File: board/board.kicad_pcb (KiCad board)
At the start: 2 copper layers, 36.5 x 17.5 mm, 41 parts, among them J2 Conn_01x10, J3 Conn_01x06, J4 Conn_01x02, J7 Conn_01x30, J8 USB_C_Receptacle_USB2.0_16P, J9 Conn_01x02, U2 nPM1300-QEAA, U3 MDBT50Q-P1MV2, U4 TVS_Array, Y1 32k Hz

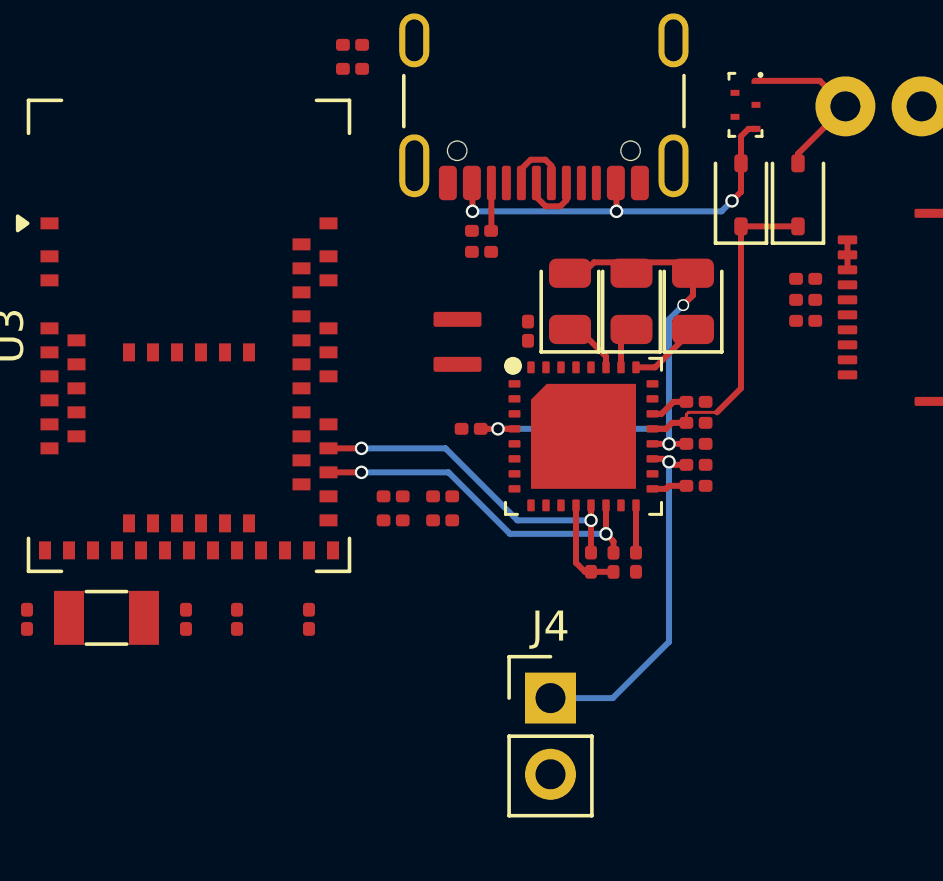
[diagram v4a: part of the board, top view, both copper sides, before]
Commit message: board: pcb route cc and vbus
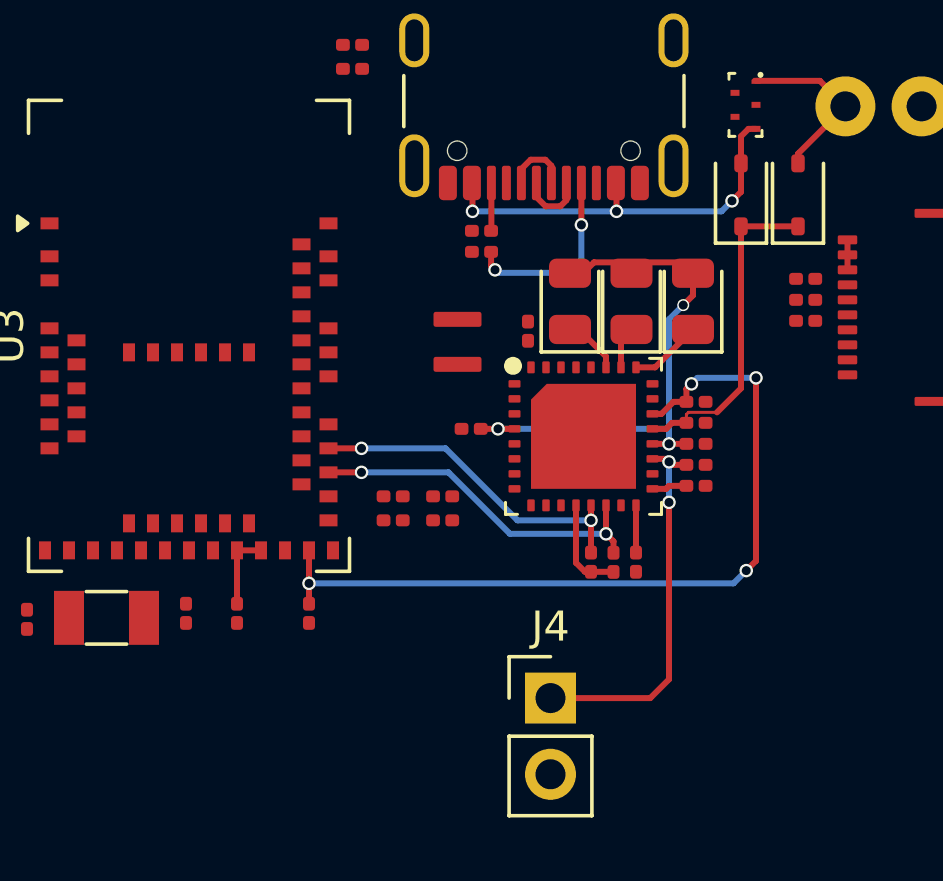
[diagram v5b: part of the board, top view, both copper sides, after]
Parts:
- moved C10 0.20 mm to (101.5, 67.2)
- moved C7 0.20 mm to (99.8, 67.2)
- moved C9 0.20 mm to (103.8, 67.2)
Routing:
- net vbus: track 1.30 -> 27.3 mm, vias 0 -> 4
- net Net-(J8-CC1): track 0.00 -> 6.33 mm, vias 0 -> 2
- net +3V3: track 3.29 -> 5.87 mm
- net vbat: track 11.9 -> 12.7 mm, vias 1 -> 2
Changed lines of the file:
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@@
 	(footprint "Capacitor_SMD:C_0201_0603Metric"
 		(layer "F.Cu")
-		(at 99.75 67.4 -90)
+		(at 99.75 67.2 -90)
 		(descr "Capacitor SMD 0201 (0603 Metric), square (rectangular) end terminal, IPC-7351 nominal, (Body size source: https://www.vishay.com/docs/20052/crcw0201e3.pdf), generated with kicad-footprint-generator")
 		(tags "capacitor")
@@
 	(footprint "Capacitor_SMD:C_0201_0603Metric"
 		(layer "F.Cu")
-		(at 103.85 67.4 -90)
+		(at 103.85 67.2 -90)
 		(descr "Capacitor SMD 0201 (0603 Metric), square (rectangular) end terminal, IPC-7351 nominal, (Body size source: https://www.vishay.com/docs/20052/crcw0201e3.pdf), generated with kicad-footprint-generator")
 		(tags "capacitor")
@@
 	(footprint "Capacitor_SMD:C_0201_0603Metric"
 		(layer "F.Cu")
-		(at 101.45 67.4 90)
+		(at 101.45 67.2 90)
 		(descr "Capacitor SMD 0201 (0603 Metric), square (rectangular) end terminal, IPC-7351 nominal, (Body size source: https://www.vishay.com/docs/20052/crcw0201e3.pdf), generated with kicad-footprint-generator")
 		(tags "capacitor")
@@
 	)
 	(segment
+		(start 103.85 66.88)
+		(end 103.85 66.2)
+		(width 0.2)
+		(layer "F.Cu")
+		(net 3)
+	)
+	(segment
+		(start 116.43 59.72)
+		(end 116.6 59.55)
+		(width 0.2)
+		(layer "F.Cu")
+		(net 3)
+	)
+	(segment
+		(start 118.75 65.45)
+		(end 118.75 59.35)
+		(width 0.2)
+		(layer "F.Cu")
+		(net 3)
+	)
+	(segment
+		(start 118.425 65.775)
+		(end 118.75 65.45)
+		(width 0.2)
+		(layer "F.Cu")
+		(net 3)
+	)
+	(segment
+		(start 116.425 60.145)
+		(end 116.43 60.15)
+		(width 0.2)
+		(layer "F.Cu")
+		(net 3)
+	)
+	(segment
+		(start 103.85 66.2)
+		(end 103.85 65.1)
+		(width 0.2)
+		(layer "F.Cu")
+		(net 3)
+	)
+	(segment
+		(start 116.43 60.15)
+		(end 116.43 59.72)
+		(width 0.2)
+		(layer "F.Cu")
+		(net 3)
+	)
+	(segment
 		(start 115.3 60.55)
 		(end 115.6 60.55)
@@
 		(net 3)
 	)
+	(via
+		(at 118.75 59.35)
+		(size 0.45)
+		(drill 0.3)
+		(layers "F.Cu" "B.Cu")
+		(net 3)
+	)
+	(via
+		(at 116.6 59.55)
+		(size 0.45)
+		(drill 0.3)
+		(layers "F.Cu" "B.Cu")
+		(net 3)
+	)
+	(via
+		(at 103.85 66.2)
+		(size 0.45)
+		(drill 0.3)
+		(layers "F.Cu" "B.Cu")
+		(net 3)
+	)
+	(via
+		(at 118.425 65.775)
+		(size 0.45)
+		(drill 0.3)
+		(layers "F.Cu" "B.Cu")
+		(net 3)
+	)
+	(segment
+		(start 118 66.2)
+		(end 103.85 66.2)
+		(width 0.2)
+		(layer "B.Cu")
+		(net 3)
+	)
+	(segment
+		(start 118.75 59.35)
+		(end 116.8 59.35)
+		(width 0.2)
+		(layer "B.Cu")
+		(net 3)
+	)
+	(segment
+		(start 116.8 59.35)
+		(end 116.6 59.55)
+		(width 0.2)
+		(layer "B.Cu")
+		(net 3)
+	)
+	(segment
+		(start 118.425 65.775)
+		(end 118 66.2)
+		(width 0.2)
+		(layer "B.Cu")
+		(net 3)
+	)
 	(segment
 		(start 115.95 60.85)
@@
 	)
 	(segment
+		(start 115.85 69.4)
+		(end 115.85 63.5)
+		(width 0.2)
+		(layer "F.Cu")
+		(net 5)
+	)
+	(segment
 		(start 115.3 62.05)
 		(end 115.75 62.05)
@@
 	)
 	(segment
+		(start 111.9 70.025)
+		(end 115.225 70.025)
+		(width 0.2)
+		(layer "F.Cu")
+		(net 5)
+	)
+	(segment
 		(start 115.95 62.25)
 		(end 116.43 62.25)
@@
 		(net 5)
 	)
+	(segment
+		(start 115.225 70.025)
+		(end 115.85 69.4)
+		(width 0.2)
+		(layer "F.Cu")
+		(net 5)
+	)
 	(via
 		(at 115.85 62.15)
@@
 		(net 5)
 	)
-	(segment
-		(start 113.975 70.025)
-		(end 111.9 70.025)
-		(width 0.2)
-		(layer "B.Cu")
+	(via
+		(at 115.85 63.5)
+		(size 0.45)
+		(drill 0.3)
+		(layers "F.Cu" "B.Cu")
 		(net 5)
 	)
 	(segment
 		(start 115.85 62.15)
-		(end 115.85 68.15)
-		(width 0.2)
-		(layer "B.Cu")
-		(net 5)
-	)
-	(segment
-		(start 115.85 68.15)
-		(end 113.975 70.025)
+		(end 115.85 63.5)
 		(width 0.2)
 		(layer "B.Cu")
@@
 	)
 	(segment
+		(start 101.45 65.1)
+		(end 101.45 66.88)
+		(width 0.2)
+		(layer "F.Cu")
+		(net 46)
+	)
+	(segment
 		(start 112.75 65.514999)
 		(end 113.050001 65.815)
@@
 	)
 	(segment
+		(start 102.25 65.1)
+		(end 101.45 65.1)
+		(width 0.2)
+		(layer "F.Cu")
+		(net 46)
+	)
+	(segment
 		(start 112.75 63.6)
 		(end 112.75 65.514999)
@@
 		(net 71)
 	)
+	(segment
+		(start 110.05 55.75)
+		(end 109.92 55.62)
+		(width 0.2)
+		(layer "F.Cu")
+		(net 74)
+	)
+	(segment
+		(start 112.93 52.855)
+		(end 112.93 54.22)
+		(width 0.2)
+		(layer "F.Cu")
+		(net 74)
+	)
+	(segment
+		(start 112.93 54.22)
+		(end 112.9 54.25)
+		(width 0.2)
+		(layer "F.Cu")
+		(net 74)
+	)
+	(segment
+		(start 109.92 55.62)
+		(end 109.92 55.15)
+		(width 0.2)
+		(layer "F.Cu")
+		(net 74)
+	)
+	(via
+		(at 110.05 55.75)
+		(size 0.45)
+		(drill 0.3)
+		(layers "F.Cu" "B.Cu")
+		(net 74)
+	)
+	(via
+		(at 112.93 54.25)
+		(size 0.45)
+		(drill 0.3)
+		(layers "F.Cu" "B.Cu")
+		(net 74)
+	)
+	(segment
+		(start 112.93 55.42)
+		(end 112.93 54.25)
+		(width 0.2)
+		(layer "B.Cu")
+		(net 74)
+	)
+	(segment
+		(start 110.05 55.75)
+		(end 110.15 55.85)
+		(width 0.2)
+		(layer "B.Cu")
+		(net 74)
+	)
+	(segment
+		(start 112.5 55.85)
+		(end 112.93 55.42)
+		(width 0.2)
+		(layer "B.Cu")
+		(net 74)
+	)
+	(segment
+		(start 110.15 55.85)
+		(end 112.5 55.85)
+		(width 0.2)
+		(layer "B.Cu")
+		(net 74)
+	)
 	(embedded_fonts no)

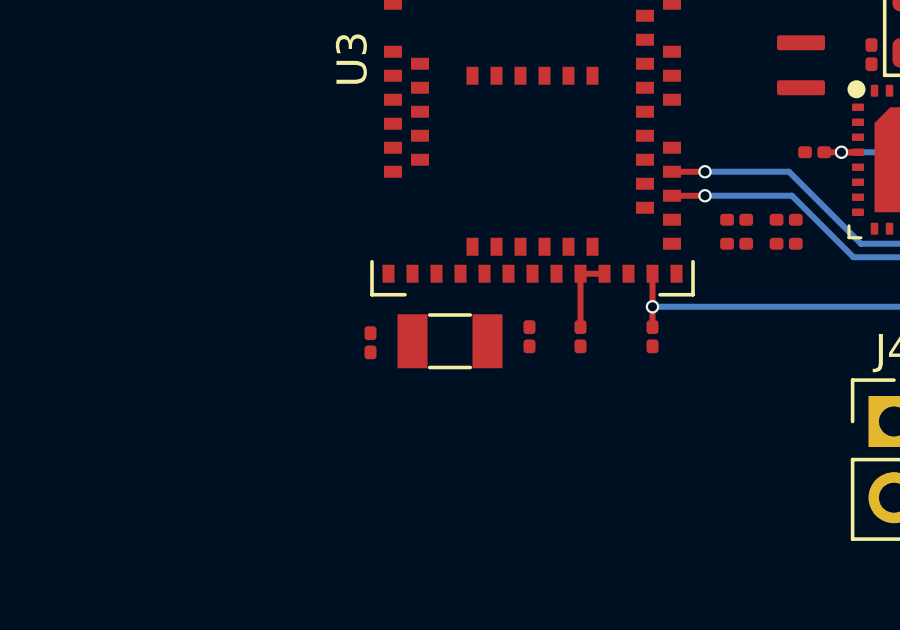
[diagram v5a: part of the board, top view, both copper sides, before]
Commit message: board: pcb route crystal
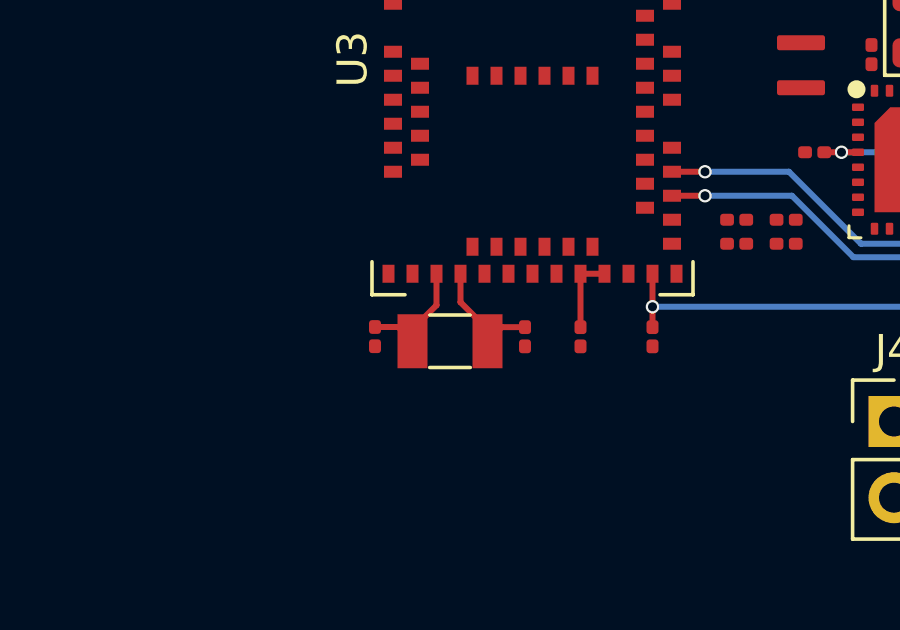
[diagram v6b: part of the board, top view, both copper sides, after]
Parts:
- moved C8 0.25 mm to (94.6, 67.2)
- moved C7 0.15 mm to (99.6, 67.2)
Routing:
- net Net-(U3-P0.01): track 0.00 -> 4.07 mm
- net Net-(U3-P0.00): track 0.00 -> 4.03 mm
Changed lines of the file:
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@@
 	(footprint "Capacitor_SMD:C_0201_0603Metric"
 		(layer "F.Cu")
-		(at 99.75 67.2 -90)
+		(at 99.6 67.2 -90)
 		(descr "Capacitor SMD 0201 (0603 Metric), square (rectangular) end terminal, IPC-7351 nominal, (Body size source: https://www.vishay.com/docs/20052/crcw0201e3.pdf), generated with kicad-footprint-generator")
 		(tags "capacitor")
@@
 	(footprint "Capacitor_SMD:C_0201_0603Metric"
 		(layer "F.Cu")
-		(at 94.45 67.4 -90)
+		(at 94.6 67.195 -90)
 		(descr "Capacitor SMD 0201 (0603 Metric), square (rectangular) end terminal, IPC-7351 nominal, (Body size source: https://www.vishay.com/docs/20052/crcw0201e3.pdf), generated with kicad-footprint-generator")
 		(tags "capacitor")
@@
 	)
 	(segment
+		(start 97.45 65.1)
+		(end 97.45 66.05)
+		(width 0.2)
+		(layer "F.Cu")
+		(net 1)
+	)
+	(segment
+		(start 98.35 67.35)
+		(end 98.82 66.88)
+		(width 0.2)
+		(layer "F.Cu")
+		(net 1)
+	)
+	(segment
+		(start 98.82 66.88)
+		(end 99.6 66.88)
+		(width 0.2)
+		(layer "F.Cu")
+		(net 1)
+	)
+	(segment
+		(start 98.35 66.95)
+		(end 98.35 67.35)
+		(width 0.2)
+		(layer "F.Cu")
+		(net 1)
+	)
+	(segment
+		(start 97.45 66.05)
+		(end 98.35 66.95)
+		(width 0.2)
+		(layer "F.Cu")
+		(net 1)
+	)
+	(segment
+		(start 96.65 66.15)
+		(end 95.85 66.95)
+		(width 0.2)
+		(layer "F.Cu")
+		(net 2)
+	)
+	(segment
+		(start 96.65 65.1)
+		(end 96.65 66.15)
+		(width 0.2)
+		(layer "F.Cu")
+		(net 2)
+	)
+	(segment
+		(start 95.85 67.35)
+		(end 95.375 66.875)
+		(width 0.2)
+		(layer "F.Cu")
+		(net 2)
+	)
+	(segment
+		(start 95.375 66.875)
+		(end 94.6 66.875)
+		(width 0.2)
+		(layer "F.Cu")
+		(net 2)
+	)
+	(segment
+		(start 95.85 66.95)
+		(end 95.85 67.35)
+		(width 0.2)
+		(layer "F.Cu")
+		(net 2)
+	)
+	(segment

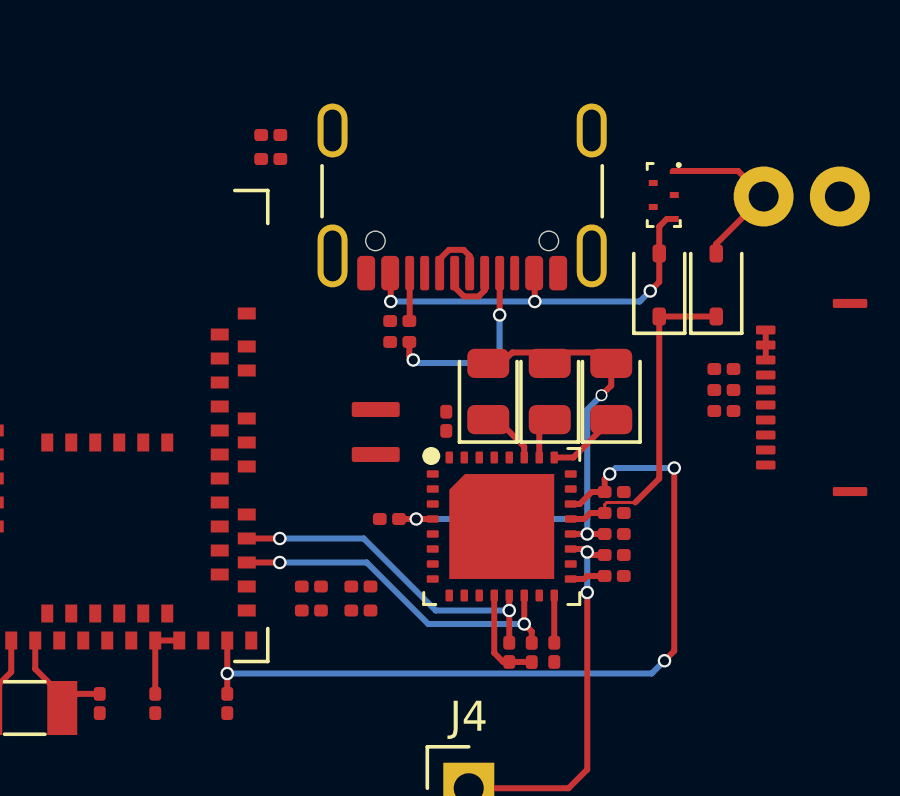
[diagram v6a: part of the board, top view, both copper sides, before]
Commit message: board: pcb route usbd+-
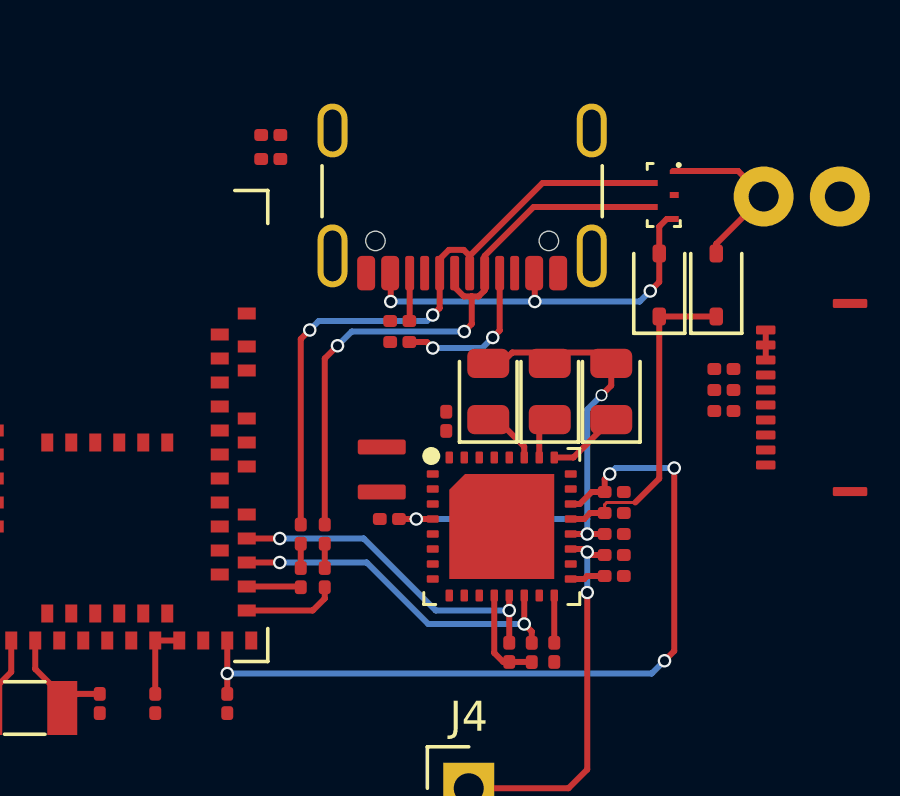
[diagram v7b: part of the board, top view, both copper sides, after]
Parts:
- moved R7 2.82 mm to (107.1, 61.6), turned to -90 degrees
- moved R9 2.66 mm to (106.3, 61.6), turned to -90 degrees
- moved L1 1.27 mm to (109.0, 59.4)
- moved R6 1.18 mm to (107.1, 63.0), turned to -90 degrees
- moved R8 0.46 mm to (106.3, 63.0), turned to -90 degrees
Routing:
- net usbd+: track 2.25 -> 21.8 mm, vias 0 -> 2
- net usbd-: track 2.25 -> 21.0 mm, vias 0 -> 2
- net Net-(U3-D-): track 0.00 -> 3.14 mm
- net Net-(U3-D+): track 0.00 -> 1.81 mm
- net Net-(J8-CC1): track 6.33 -> 5.37 mm
- net Net-(R8-Pad1): track 0.00 -> 0.81 mm
- net Net-(R6-Pad1): track 0.00 -> 0.81 mm
